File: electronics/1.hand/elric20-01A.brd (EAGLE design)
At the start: 113.1 x 72.2 mm, 30 parts

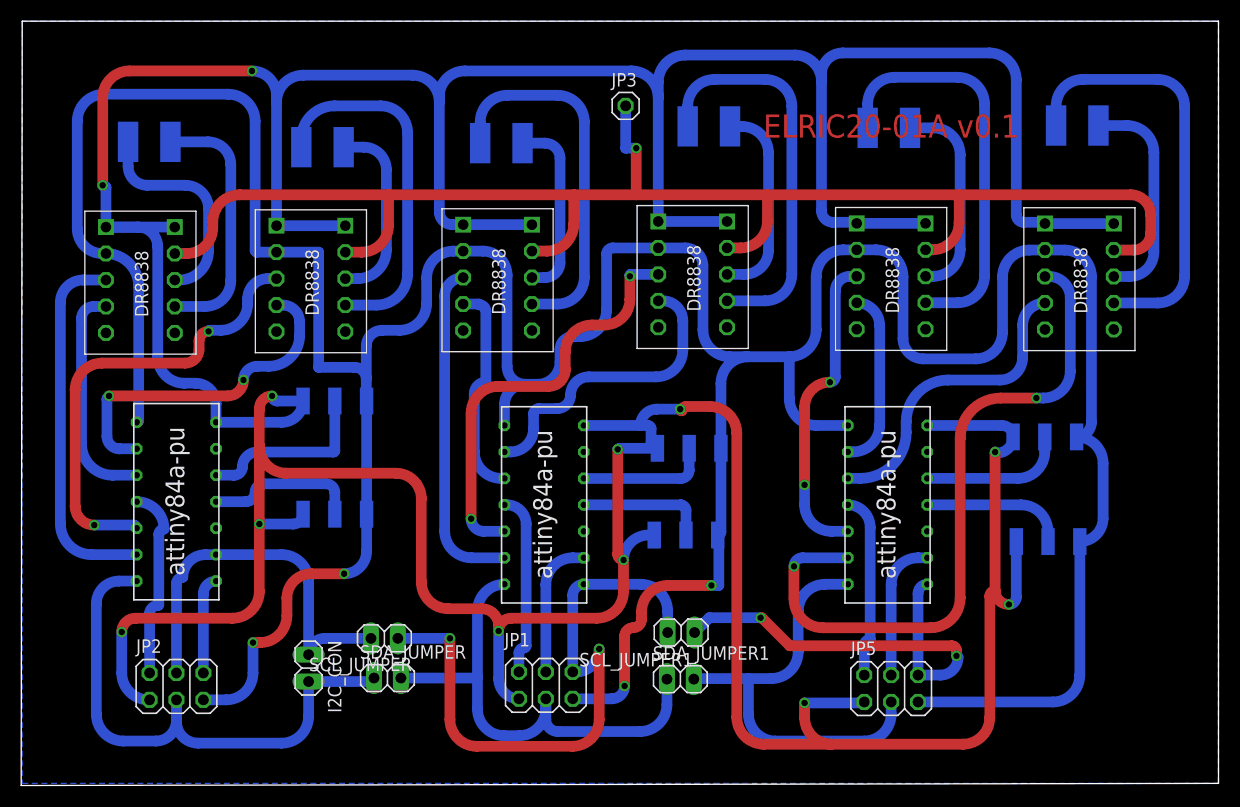
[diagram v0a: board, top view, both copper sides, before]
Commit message: New version of hand electronics. Packed in servos 2 by 2
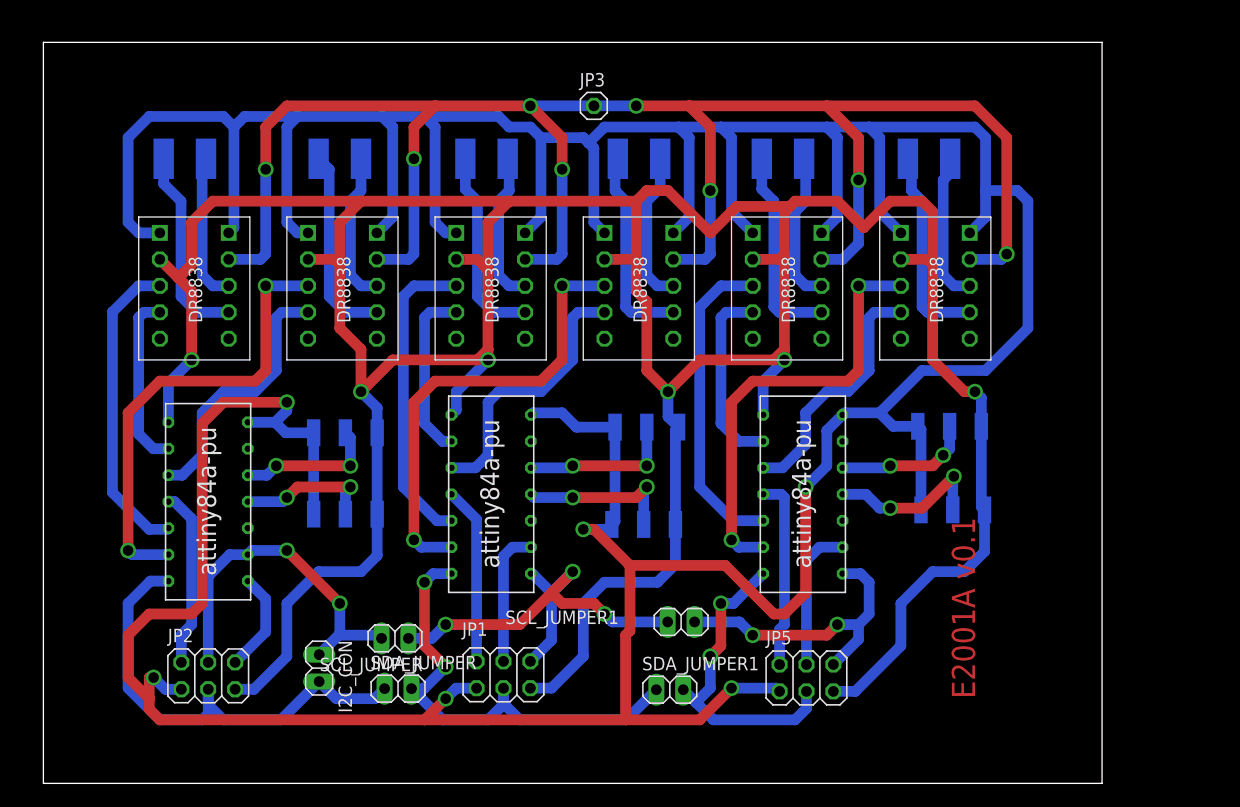
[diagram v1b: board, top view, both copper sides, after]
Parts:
- moved U$11 21.2 mm to (39.9, 59.0)
- moved U$4 19.1 mm to (39.0, 52.0)
- moved U$7 19.1 mm to (25.0, 52.0)
- moved U$10 14.3 mm to (81.7, 59.0)
- moved U$14 14.1 mm to (26.0, 59.0), turned to 90 degrees
- moved U$3 13.6 mm to (81.0, 52.0)
- moved U$5 13.4 mm to (53.0, 52.0)
- moved U$12 13.1 mm to (54.3, 59.0)
- moved U$13 13.0 mm to (11.4, 59.0)
- moved U$6 11.0 mm to (11.0, 52.0)
- moved U$9 10.4 mm to (67.9, 59.0)
- moved U$2 9.87 mm to (67.0, 52.0)
- moved U$19 9.49 mm to (85.9, 25.8)
- moved U$20 9.06 mm to (85.6, 33.7)
- moved JP5 8.06 mm to (72.1, 9.96)
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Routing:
- net N$13: track 140.9 -> 176.9 mm, vias 1 -> 8
- net GND: track 506.5 -> 476.9 mm, vias 12 -> 6
- net PWM_2: track 64.8 -> 41.5 mm
- net N$4: track 39.8 -> 19.3 mm
- net N$2: track 38.2 -> 19.2 mm
- net N$6: track 36.9 -> 18.6 mm
- net MISO_1: track 58.6 -> 43.1 mm, vias 2 -> 3
- net N$8: track 34.6 -> 19.2 mm
- net DIR_5: track 31.7 -> 16.6 mm, vias 2 -> 0
- net N$10: track 33.6 -> 18.8 mm
- net PWM_5: track 41.8 -> 29.3 mm, vias 2 -> 0
- net MISO_3: track 40.7 -> 28.4 mm
- net PWM_4: track 31.4 -> 43.5 mm, vias 0 -> 2
- net DIR_3: track 27.5 -> 16.5 mm
- net MOSI_3: track 40.6 -> 30.4 mm, vias 0 -> 2
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- removed copper zone on layer 16, net GND
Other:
- board size 113.1 x 72.2 mm -> 100 x 70 mm
- board text added: "E2001A v0.1"
- board text removed: "ELRIC20-01A v0.1"
